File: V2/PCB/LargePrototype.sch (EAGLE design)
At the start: 231 parts, among them U1 GENERIC-SOIC8, U2 GENERIC-SOIC8, U3 GENERIC-SOIC8, U4 GENERIC-SOIC8

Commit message: Minor fixes for location of silk screen.
Added pdf's and images of pcb/schematic.

Added to DirtyPCBs order.
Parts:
- removed JP32: Alignment, SparkFun-Connectors:M30
- removed JP8: Alignment, SparkFun-Connectors:M10NO_SILK_PTH_FEMALE
- added LOGO2: OSHW-LOGOL, SparkFun-Aesthetics:OSHW-LOGOL
- added LOGO3: OSHW-LOGOM, SparkFun-Aesthetics:OSHW-LOGOM
- JP16: value 3v3 -> (none)
- JP33: value GND -> (none)
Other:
- moved on the sheet: JP108, JP111, JP112, JP113, JP114, JP115, JP116, JP117, JP118, JP31, JP34, JP35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

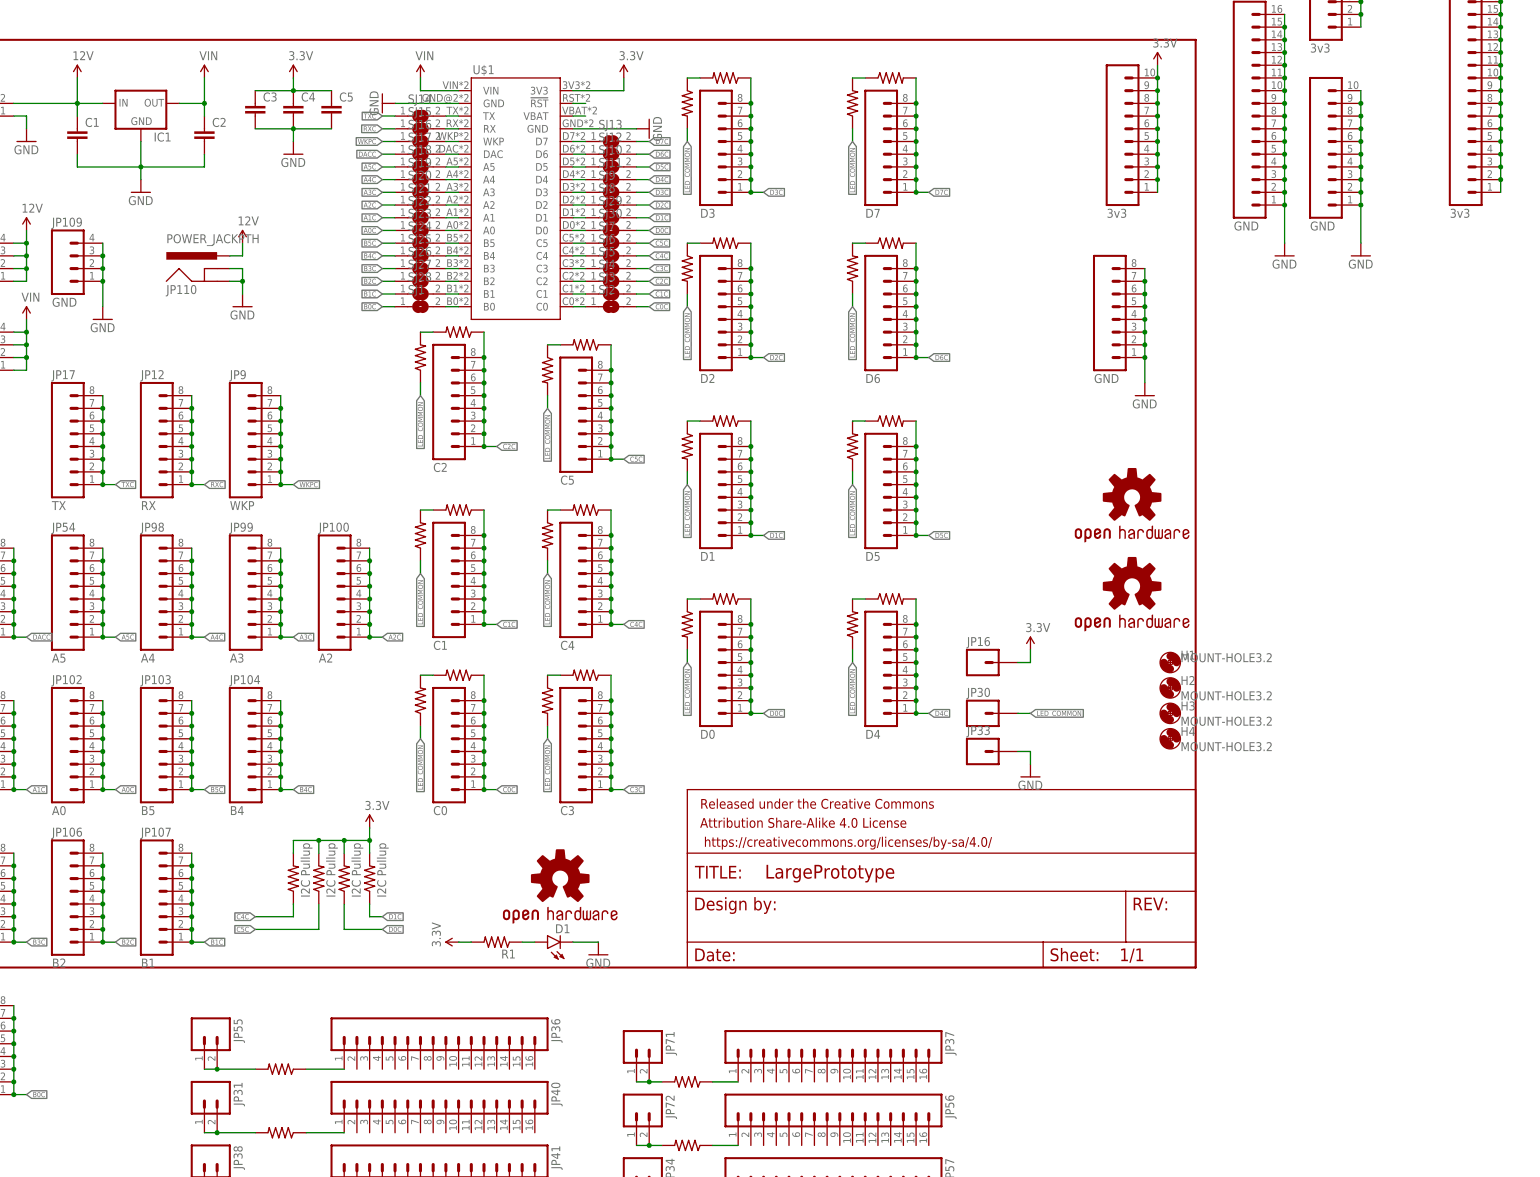
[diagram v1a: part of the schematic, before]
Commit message: Relabelled large electron prototype as V2 to match the folder.
Improved silk screen

Removed jumper links for electron pins so they are connected through

Added a couple more capacitor places.

Added 3v3 and GND links to lower half board edge
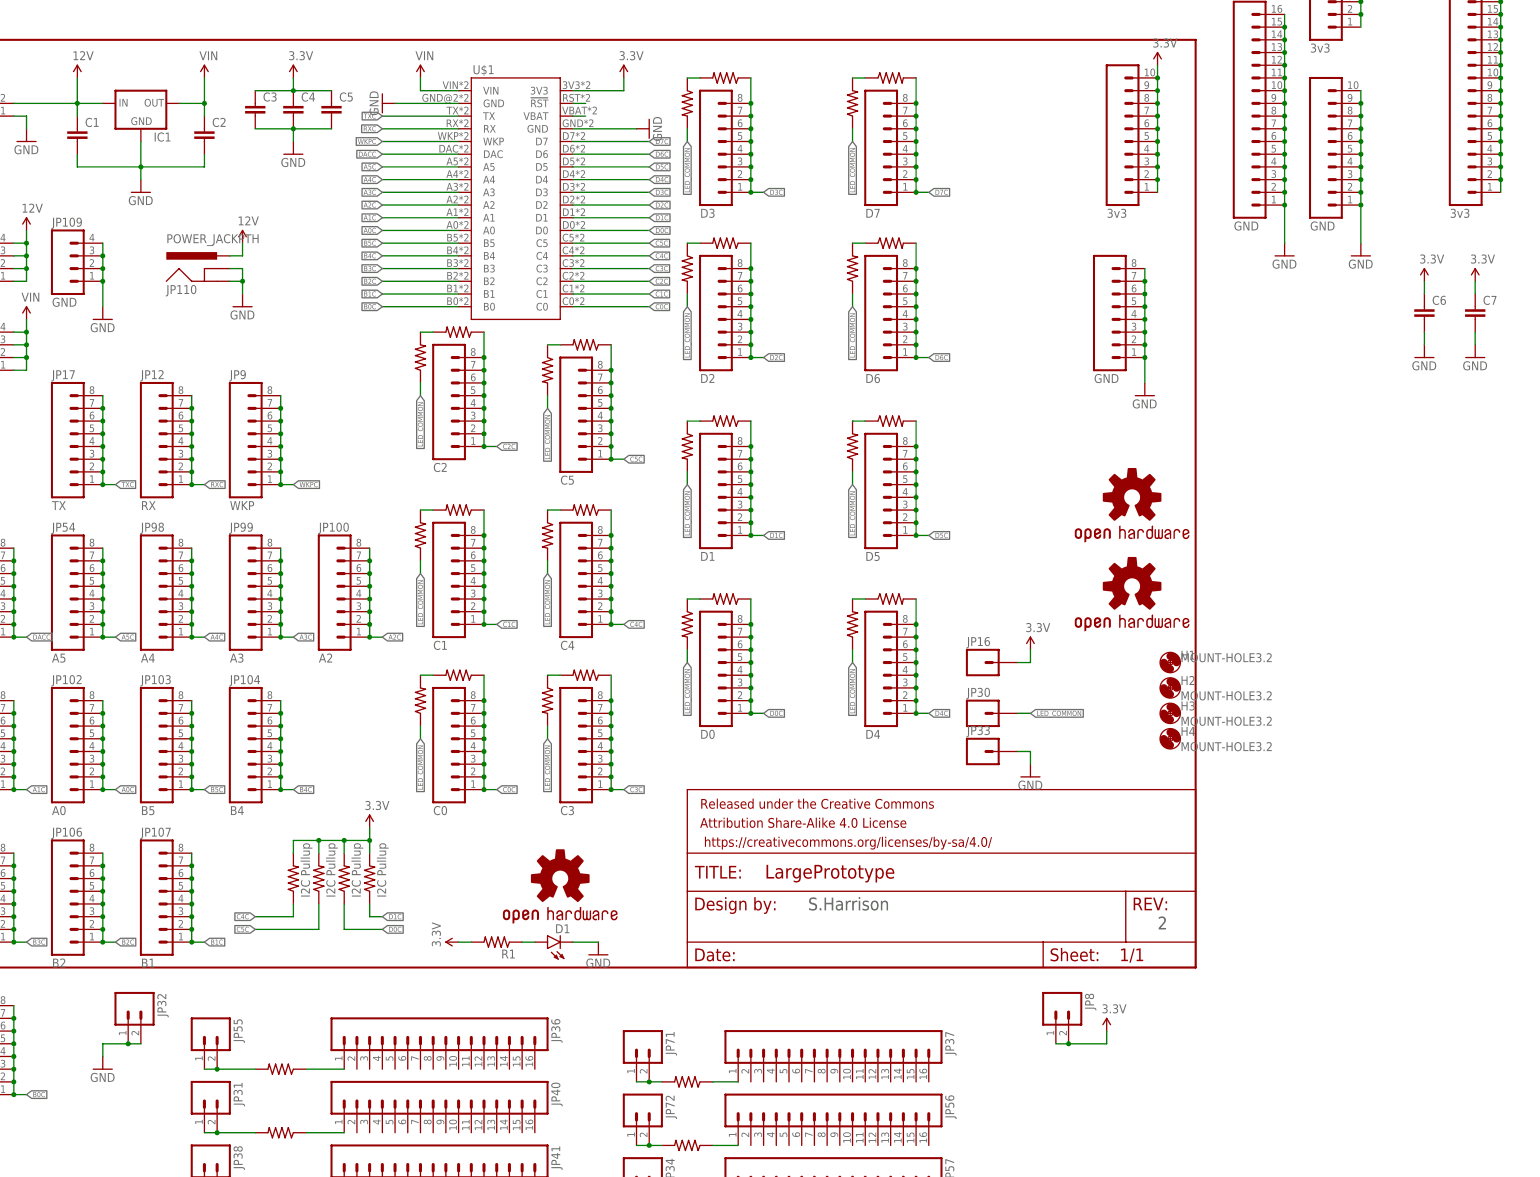
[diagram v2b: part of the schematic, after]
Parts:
- removed SJ1, SJ10, SJ11, SJ12, SJ13, SJ14, SJ15, SJ16, SJ17, SJ18, SJ19, SJ2, SJ20, SJ21, SJ22, SJ23, SJ24, SJ25, SJ26, SJ27, SJ28, SJ29, SJ3, SJ30, SJ4, SJ5, SJ6, SJ7, SJ8, SJ9: (no value), jumper:SJ
- added C6, C7: (no value), SparkFun-Capacitors:1UF-25V-10%(0805)"
- added JP32, JP8: (no value), SparkFun-Connectors:M02PTH
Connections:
- removed net C4: SJ6.1, U$1.C4
- removed net C5: SJ7.1, U$1.C5
- removed net D0: SJ30.1, U$1.D0
- removed net D1: SJ29.1, U$1.D1
- removed net N$100: SJ4.1, U$1.C2
- removed net N$101: SJ3.1, U$1.C1
- removed net N$102: SJ2.1, U$1.C0
- removed net N$103: SJ8.1, U$1.D2
- removed net N$105: SJ9.1, U$1.D3
- removed net N$106: SJ11.1, U$1.D4
- removed net N$107: SJ10.1, U$1.D5
- removed net N$108: SJ12.1, U$1.D6
- removed net N$109: SJ13.1, U$1.D7
- removed net N$112: SJ14.2, U$1.TX
- removed net N$113: SJ15.2, U$1.RX
- removed net N$114: SJ16.2, U$1.WKP
- removed net N$115: SJ17.2, U$1.DAC
- removed net N$116: SJ18.2, U$1.A5
- removed net N$117: SJ19.2, U$1.A4
- removed net N$118: SJ20.2, U$1.A3
- removed net N$119: SJ21.2, U$1.A2
- removed net N$120: SJ22.2, U$1.A1
- removed net N$121: SJ23.2, U$1.A0
- removed net N$122: SJ24.2, U$1.B5
- removed net N$123: SJ25.2, U$1.B4
- removed net N$124: SJ26.2, U$1.B3
- removed net N$125: SJ27.2, U$1.B2
- removed net N$126: SJ28.2, U$1.B1
- removed net N$127: SJ1.2, U$1.B0
- removed net N$99: SJ5.1, U$1.C3
- net 3.3V: now also C6.1, C7.1, JP8.1, JP8.2
- net A0C: now also U$1.A0; no longer SJ23.1
- net A1C: now also U$1.A1; no longer SJ22.1
- net A2C: now also U$1.A2; no longer SJ21.1
- net A3C: now also U$1.A3; no longer SJ20.1
- net A4C: now also U$1.A4; no longer SJ19.1
- net A5C: now also U$1.A5; no longer SJ18.1
- net B0C: now also U$1.B0; no longer SJ1.1
- net B1C: now also U$1.B1; no longer SJ28.1
- net B2C: now also U$1.B2; no longer SJ27.1
- net B3C: now also U$1.B3; no longer SJ26.1
- net B4C: now also U$1.B4; no longer SJ25.1
- net B5C: now also U$1.B5; no longer SJ24.1
- net C0C: now also U$1.C0; no longer SJ2.2
- net C1C: now also U$1.C1; no longer SJ3.2
- net C2C: now also U$1.C2; no longer SJ4.2
- net C3C: now also U$1.C3; no longer SJ5.2
- net C4C: now also U$1.C4; no longer SJ6.2
- net C5C: now also U$1.C5; no longer SJ7.2
- net D0C: now also U$1.D0; no longer SJ30.2
- net D1C: now also U$1.D1; no longer SJ29.2
- net D2C: now also U$1.D2; no longer SJ8.2
- net D3C: now also U$1.D3; no longer SJ9.2
- net D4C: now also U$1.D4; no longer SJ11.2
- net D5C: now also U$1.D5; no longer SJ10.2
- net D6C: now also U$1.D6; no longer SJ12.2
- net D7C: now also U$1.D7; no longer SJ13.2
- net DACC: now also U$1.DAC; no longer SJ17.1
- net GND: now also C6.2, C7.2, JP32.1, JP32.2
- net RXC: now also U$1.RX; no longer SJ15.1
- net TXC: now also U$1.TX; no longer SJ14.1
- net WKPC: now also U$1.WKP; no longer SJ16.1
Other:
- note added: "2"
- note added: "S.Harrison"
